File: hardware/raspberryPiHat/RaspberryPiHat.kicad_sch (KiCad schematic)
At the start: 12 parts, among them J1 Raspberry_Pi_2_3, J2 Conn_01x04_Socket, J3 Conn_01x02_Pin, SW1 SW_Push, U1 ESP32-WROOM-32U

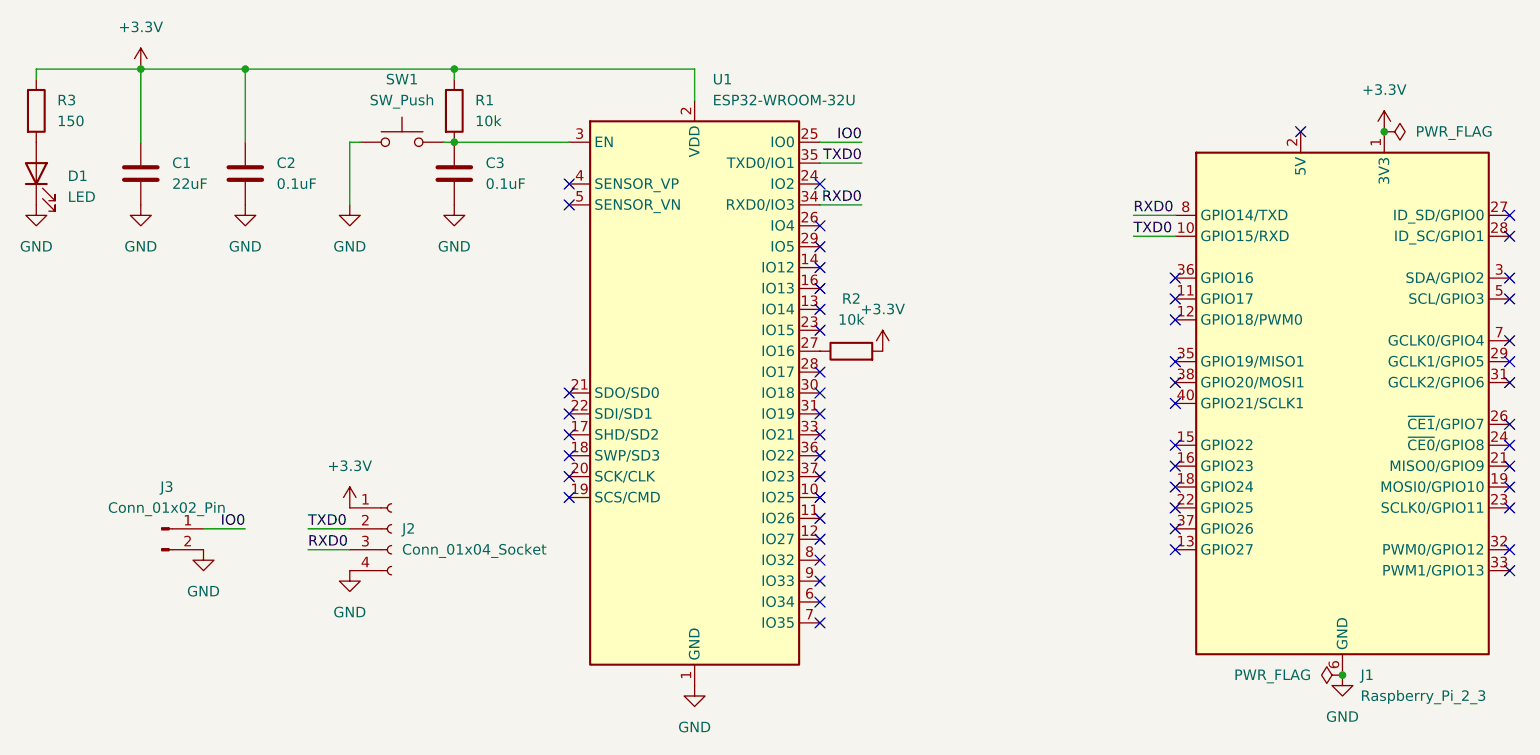
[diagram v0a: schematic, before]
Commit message: updated rpi
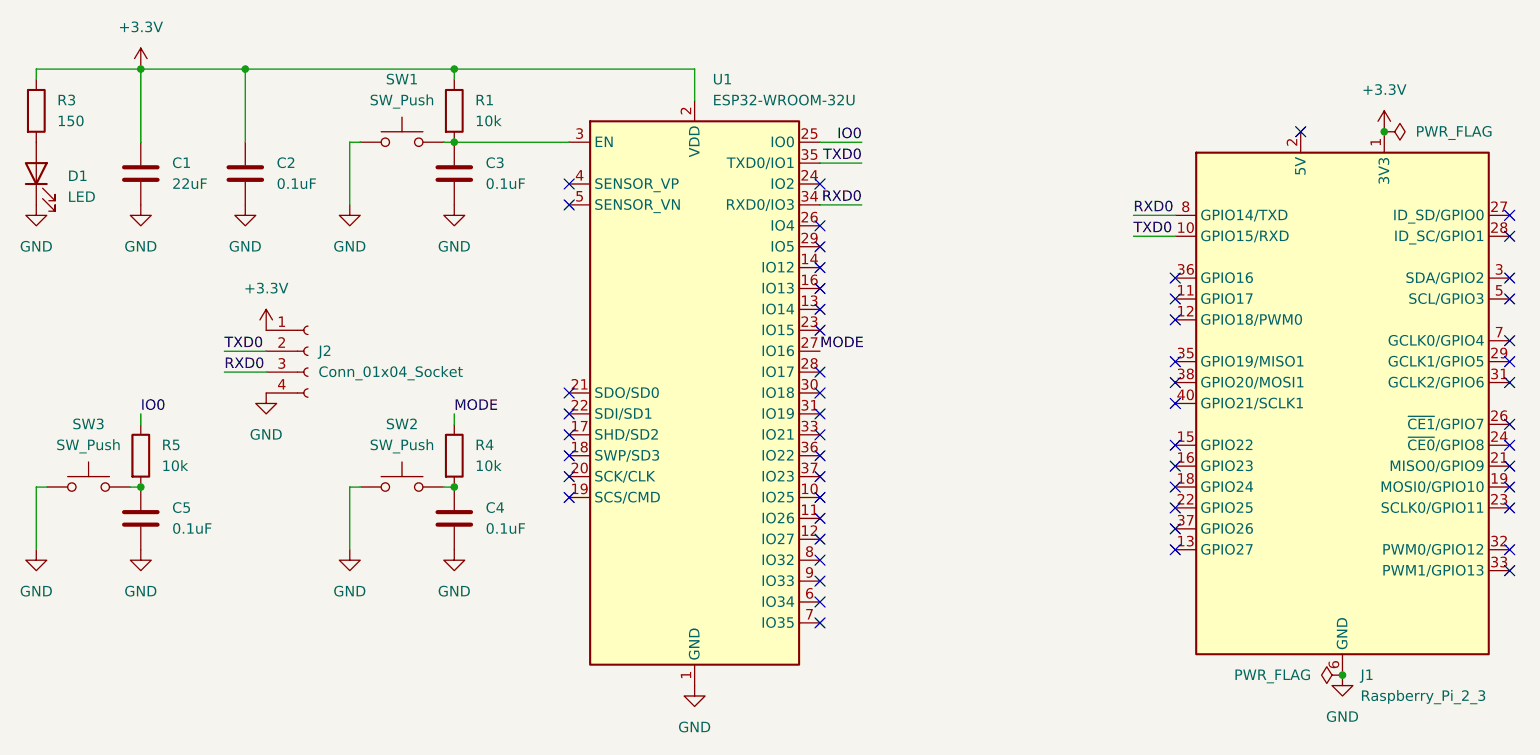
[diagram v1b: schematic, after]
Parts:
- removed J3: Conn_01x02_Pin, Connector_PinHeader_2.54mm:PinHeader_1x02_P2.54mm_Vertical, symbol Connector:Conn_01x02_Pin
- removed R2: 10k, Resistor_SMD:R_0603_1608Metric, symbol Device:R
- added C4, C5: 0.1uF, Capacitor_SMD:C_0603_1608Metric, symbol Device:C
- added R4, R5: 10k, Resistor_SMD:R_0603_1608Metric, symbol Device:R
- added SW2, SW3: SW_Push, Button_Switch_THT:SW_PUSH_6mm, symbol Switch:SW_Push
- SW1: footprint Buttons_Switches_THT.pretty-master:SW_PUSH_6mm -> Button_Switch_THT:SW_PUSH_6mm
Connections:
- net GND: now also C4.2, C5.2, SW2.1, SW3.1
- net IO0: now also R5.1
- net MODE: now reaches U1.27 (IO16)
- net MODE: now also R4.1
- new net: C5.1, R5.2, SW3.2
- new net: C4.1, R4.2, SW2.2
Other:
- moved on the sheet: J2
